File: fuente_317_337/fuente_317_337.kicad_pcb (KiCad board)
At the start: 2 copper layers, 80 x 61 mm, 52 parts, among them J1 Fuente, J10 SEL_7905, J11 -5, J12 ADC+, J13 ADC-, J2 Salida, J3 Salida_12v, J4 Cooler, J5 +5, J6 GND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

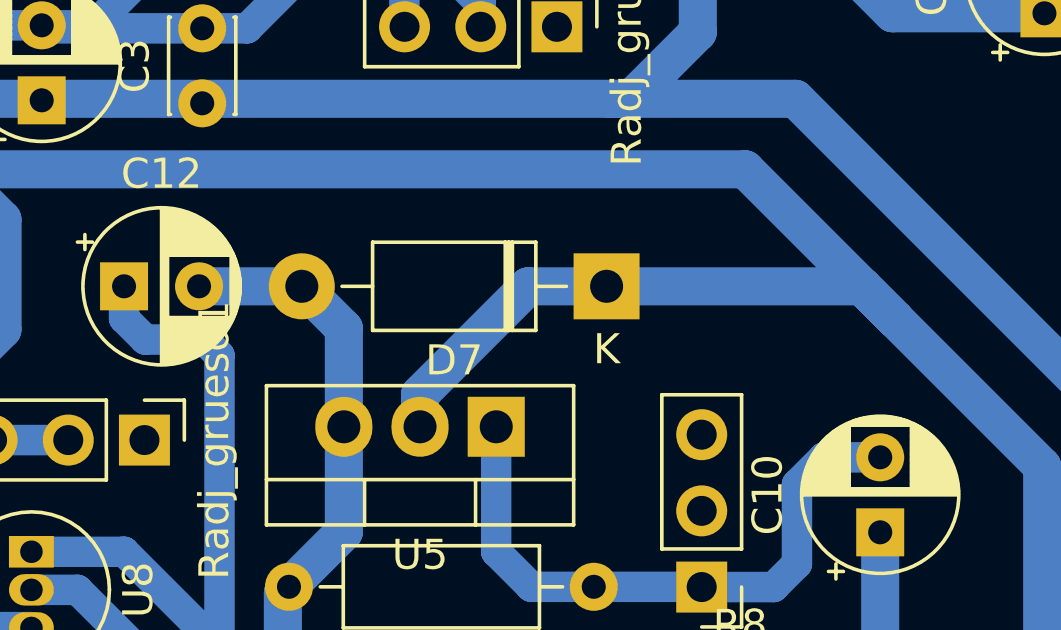
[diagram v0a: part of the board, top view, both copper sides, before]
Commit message: fix: protection diode
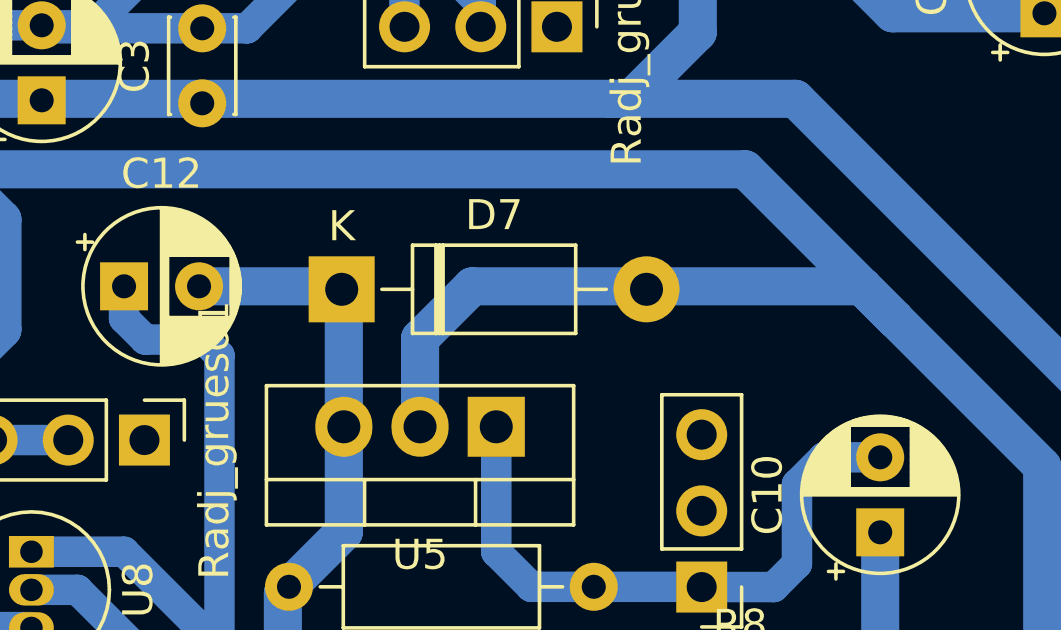
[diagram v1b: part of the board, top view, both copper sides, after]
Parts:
- moved D7 8.83 mm to (58.5, 45.1), turned to 0 degrees
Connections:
- D7 pad 1: -12V -> Io1-
- D7 pad 2: Io1- -> -12V
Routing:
- net -12V: track 169.4 -> 170.5 mm
- net Io1-: track 35.7 -> 36.4 mm
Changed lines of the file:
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@@
 	(footprint "Diode_THT:D_DO-41_SOD81_P10.16mm_Horizontal"
 		(layer "F.Cu")
-		(at 67.28 45 180)
+		(at 58.45 45.1)
 		(descr "Diode, DO-41_SOD81 series, Axial, Horizontal, pin pitch=10.16mm, , length*diameter=5.2*2.7mm^2, , http://www.diodes.com/_files/packages/DO-41%20(Plastic).pdf")
 		(tags "Diode DO-41_SOD81 series Axial Horizontal pin pitch 10.16mm  length 5.2mm diameter 2.7mm")
 		(property "Reference" "D7"
-			(at 5.08 -2.47 180)
+			(at 5.08 -2.47 360)
 			(layer "F.SilkS")
 			(effects
@@
 		)
 		(property "Value" "1N4007"
-			(at 5.08 2.47 180)
+			(at 5.08 2.47 360)
 			(layer "F.Fab")
 			(effects
@@
 		)
 		(property "Footprint" "Diode_THT:D_DO-41_SOD81_P10.16mm_Horizontal"
-			(at 0 0 180)
+			(at 0 0 0)
 			(unlocked yes)
 			(layer "F.Fab")
@@
 		)
 		(property "Datasheet" "http://www.vishay.com/docs/88503/1n4001.pdf"
-			(at 0 0 180)
+			(at 0 0 0)
 			(unlocked yes)
 			(layer "F.Fab")
@@
 		)
 		(property "Description" "1000V 1A General Purpose Rectifier Diode, DO-41"
-			(at 0 0 180)
+			(at 0 0 0)
 			(unlocked yes)
 			(layer "F.Fab")
@@
 		)
 		(property "Sim.Device" "D"
-			(at 0 0 180)
+			(at 0 0 0)
 			(unlocked yes)
 			(layer "F.Fab")
@@
 		)
 		(property "Sim.Pins" "1=K 2=A"
-			(at 0 0 180)
+			(at 0 0 0)
 			(unlocked yes)
 			(layer "F.Fab")
@@
 		(attr through_hole)
 		(fp_line
-			(start 8.82 0)
-			(end 7.8 0)
+			(start 1.34 0)
+			(end 2.36 0)
 			(stroke
 				(width 0.12)
@@
 		)
 		(fp_line
-			(start 7.8 1.47)
-			(end 7.8 -1.47)
+			(start 2.36 -1.47)
+			(end 2.36 1.47)
 			(stroke
 				(width 0.12)
@@
 		)
 		(fp_line
-			(start 7.8 -1.47)
-			(end 2.36 -1.47)
+			(start 2.36 1.47)
+			(end 7.8 1.47)
 			(stroke
 				(width 0.12)
@@
 		)
 		(fp_line
-			(start 3.38 -1.47)
-			(end 3.38 1.47)
+			(start 3.14 -1.47)
+			(end 3.14 1.47)
 			(stroke
 				(width 0.12)
@@
 		)
 		(fp_line
-			(start 3.14 -1.47)
-			(end 3.14 1.47)
+			(start 3.38 -1.47)
+			(end 3.38 1.47)
 			(stroke
 				(width 0.12)
@@
 		)
 		(fp_line
-			(start 2.36 1.47)
-			(end 7.8 1.47)
+			(start 7.8 -1.47)
+			(end 2.36 -1.47)
 			(stroke
 				(width 0.12)
@@
 		)
 		(fp_line
-			(start 2.36 -1.47)
-			(end 2.36 1.47)
+			(start 7.8 1.47)
+			(end 7.8 -1.47)
 			(stroke
 				(width 0.12)
@@
 		)
 		(fp_line
-			(start 1.34 0)
-			(end 2.36 0)
+			(start 8.82 0)
+			(end 7.8 0)
 			(stroke
 				(width 0.12)
@@
 		)
 		(fp_line
-			(start 11.51 1.6)
-			(end 11.51 -1.6)
+			(start -1.35 -1.6)
+			(end -1.35 1.6)
 			(stroke
 				(width 0.05)
@@
 		)
 		(fp_line
-			(start 11.51 -1.6)
-			(end -1.35 -1.6)
+			(start -1.35 1.6)
+			(end 11.51 1.6)
 			(stroke
 				(width 0.05)
@@
 		)
 		(fp_line
-			(start -1.35 1.6)
-			(end 11.51 1.6)
+			(start 11.51 -1.6)
+			(end -1.35 -1.6)
 			(stroke
 				(width 0.05)
@@
 		)
 		(fp_line
-			(start -1.35 -1.6)
-			(end -1.35 1.6)
+			(start 11.51 1.6)
+			(end 11.51 -1.6)
 			(stroke
 				(width 0.05)
@@
 		)
 		(fp_line
-			(start 10.16 0)
-			(end 7.68 0)
+			(start 0 0)
+			(end 2.48 0)
 			(stroke
 				(width 0.1)
@@
 		)
 		(fp_line
-			(start 7.68 1.35)
-			(end 7.68 -1.35)
+			(start 2.48 -1.35)
+			(end 2.48 1.35)
 			(stroke
 				(width 0.1)
@@
 		)
 		(fp_line
-			(start 7.68 -1.35)
-			(end 2.48 -1.35)
+			(start 2.48 1.35)
+			(end 7.68 1.35)
 			(stroke
 				(width 0.1)
@@
 		)
 		(fp_line
-			(start 3.36 -1.35)
-			(end 3.36 1.35)
+			(start 3.16 -1.35)
+			(end 3.16 1.35)
 			(stroke
 				(width 0.1)
@@
 		)
 		(fp_line
-			(start 3.16 -1.35)
-			(end 3.16 1.35)
+			(start 3.36 -1.35)
+			(end 3.36 1.35)
 			(stroke
 				(width 0.1)
@@
 		)
 		(fp_line
-			(start 2.48 1.35)
-			(end 7.68 1.35)
+			(start 7.68 -1.35)
+			(end 2.48 -1.35)
 			(stroke
 				(width 0.1)
@@
 		)
 		(fp_line
-			(start 2.48 -1.35)
-			(end 2.48 1.35)
+			(start 7.68 1.35)
+			(end 7.68 -1.35)
 			(stroke
 				(width 0.1)
@@
 		)
 		(fp_line
-			(start 0 0)
-			(end 2.48 0)
+			(start 10.16 0)
+			(end 7.68 0)
 			(stroke
 				(width 0.1)
@@
 		)
 		(fp_text user "K"
-			(at 0 -2.1 180)
+			(at 0 -2.1 360)
 			(layer "F.SilkS")
 			(effects
@@
 		)
 		(fp_text user "${REFERENCE}"
-			(at 5.47 0 180)
+			(at 5.47 0 360)
 			(layer "F.Fab")
 			(effects
@@
 		)
 		(fp_text user "K"
-			(at 0 -2.1 180)
+			(at 0 -2.1 360)
 			(layer "F.Fab")
 			(effects
@@
 		)
 		(pad "1" thru_hole rect
-			(at 0 0 180)
+			(at 0 0)
 			(size 2.2 2.2)
 			(drill 1.1)
 			(layers "*.Cu" "*.Mask")
 			(remove_unused_layers no)
-			(net 3 "-12V")
+			(net 9 "Io1-")
 			(pinfunction "K")
 			(pintype "passive")
 		)
 		(pad "2" thru_hole oval
-			(at 10.16 0 180)
+			(at 10.16 0)
 			(size 2.2 2.2)
 			(drill 1.1)
 			(layers "*.Cu" "*.Mask")
 			(remove_unused_layers no)
-			(net 9 "Io1-")
+			(net 3 "-12V")
 			(pinfunction "A")
 			(pintype "passive")
@@
 		)
 		(height 8.425)
-		(gr_text "61.0000 mm"
+		(gr_text "61,0000 mm"
 			(at 107.275 44.5 90)
 			(layer "User.1")
@@
 		)
 		(height 6.875)
-		(gr_text "80.0000 mm"
+		(gr_text "80,0000 mm"
 			(at 60 80.725 0)
 			(layer "User.1")
@@
 	)
 	(segment
+		(start 62.8 45)
+		(end 75.8 45)
+		(width 1.27)
+		(layer "B.Cu")
+		(net 3)
+	)
+	(segment
 		(start 76.9 46.1)
 		(end 81.8 51)
@@
 	)
 	(segment
+		(start 75.8 45)
+		(end 76.9 46.1)
+		(width 1.27)
+		(layer "B.Cu")
+		(net 3)
+	)
+	(segment
 		(start 46.4024 61.49)
 		(end 46.3804 61.468)
@@
 	)
 	(segment
-		(start 61.0616 49.6824)
-		(end 61.0616 48.5999)
-		(width 1.27)
-		(layer "B.Cu")
-		(net 3)
-	)
-	(segment
 		(start 36.24 69.11)
 		(end 40.28 69.11)
@@
 	)
 	(segment
-		(start 64.6615 45)
-		(end 67.28 45)
-		(width 1.27)
-		(layer "B.Cu")
-		(net 3)
-	)
-	(segment
 		(start 78.2828 62.3172)
 		(end 78.2828 70.23)
@@
 	)
 	(segment
-		(start 67.28 45)
-		(end 75.8 45)
-		(width 1.27)
-		(layer "B.Cu")
-		(net 3)
-	)
-	(segment
 		(start 50.2412 63.9064)
 		(end 50.2412 60.9092)
@@
 	)
 	(segment
-		(start 44.4754 40.1066)
-		(end 45.4688 41.1)
+		(start 61.0616 46.7384)
+		(end 62.8 45)
 		(width 1.27)
 		(layer "B.Cu")
@@
 	)
 	(segment
-		(start 43.35 58.43)
-		(end 40.11 55.19)
+		(start 44.4754 40.1066)
+		(end 45.4688 41.1)
 		(width 1.27)
 		(layer "B.Cu")
@@
 	)
 	(segment
-		(start 75.8 45)
-		(end 76.9 46.1)
+		(start 43.35 58.43)
+		(end 40.11 55.19)
 		(width 1.27)
 		(layer "B.Cu")
@@
 	)
 	(segment
-		(start 61.0616 48.5999)
-		(end 64.6615 45)
+		(start 61.0616 49.6824)
+		(end 61.0616 46.7384)
 		(width 1.27)
 		(layer "B.Cu")
@@
 	)
 	(segment
-		(start 53.694888 45)
-		(end 57.12 45)
+		(start 58.5216 45.1716)
+		(end 58.5216 49.6824)
 		(width 1.27)
 		(layer "B.Cu")
@@
 	)
 	(segment
-		(start 57.12 45)
-		(end 58.5216 46.4016)
+		(start 56.6928 55.0164)
+		(end 56.4896 55.2196)
 		(width 1.27)
 		(layer "B.Cu")
@@
 	)
 	(segment
-		(start 56.6928 55.0164)
-		(end 56.4896 55.2196)
+		(start 58.5216 53.1876)
+		(end 56.6928 55.0164)
 		(width 1.27)
 		(layer "B.Cu")
@@
 	)
 	(segment
-		(start 58.5216 53.1876)
-		(end 56.6928 55.0164)
+		(start 58.45 45.1)
+		(end 58.5216 45.1716)
 		(width 1.27)
 		(layer "B.Cu")
@@
 	)
 	(segment
-		(start 58.5216 46.4016)
-		(end 58.5216 49.6824)
+		(start 58.35 45)
+		(end 58.45 45.1)
+		(width 1.27)
+		(layer "B.Cu")
+		(net 9)
+	)
+	(segment
+		(start 53.694888 45)
+		(end 58.35 45)
 		(width 1.27)
 		(layer "B.Cu")
